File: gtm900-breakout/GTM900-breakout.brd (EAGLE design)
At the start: 70 x 70 mm, 97 parts, among them J1 AUDIO-JACK3, K1 PJ-002BH-SMT-TR, T1 BC847, T2 BC847, T3 BC847, T4 BC847, U1 FH12A-40S-0.5SH(55), U2 MCP1827T-ADJE/ET, U3 MIC5366, U4 CP2105-GM, U5 IP4234CZ6, X4 MINI-USB-SHIELD-UX60-MB-5ST

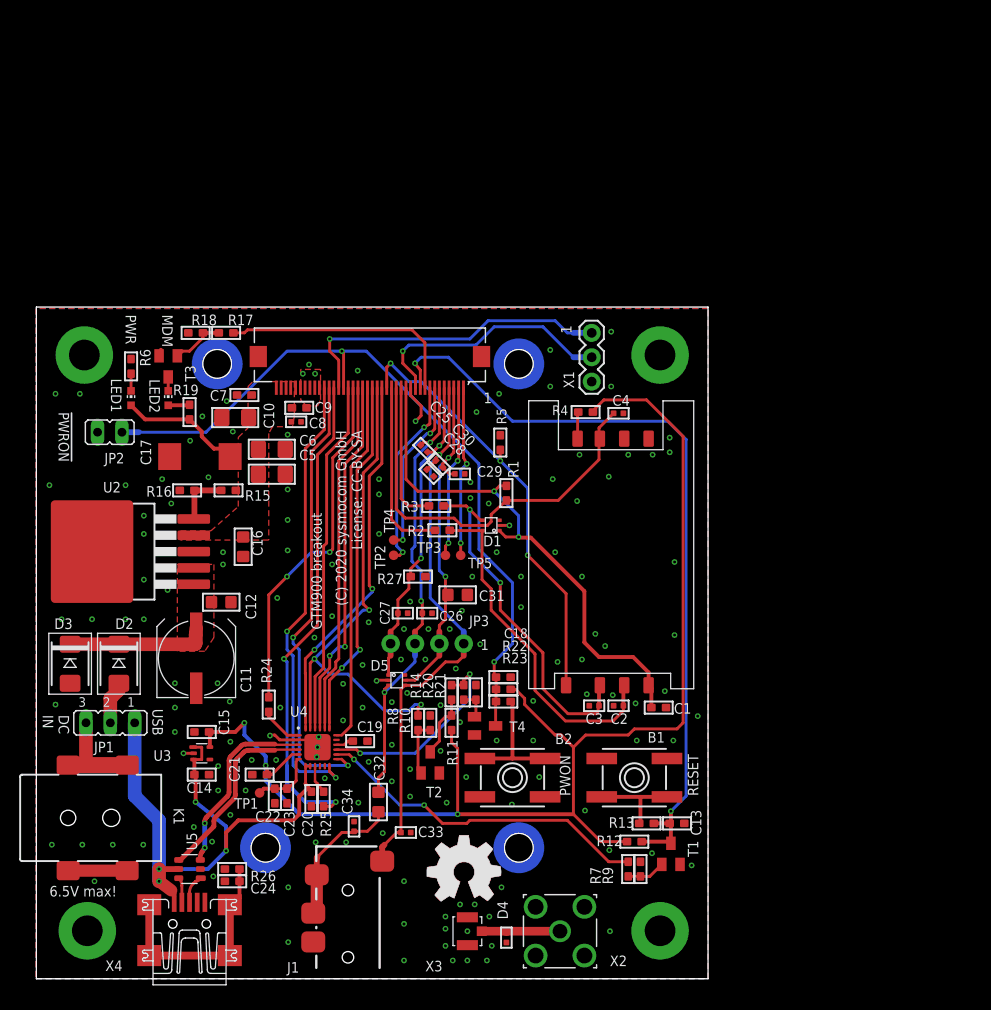
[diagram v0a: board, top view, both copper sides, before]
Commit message: GTM900-breakout: add next design v2
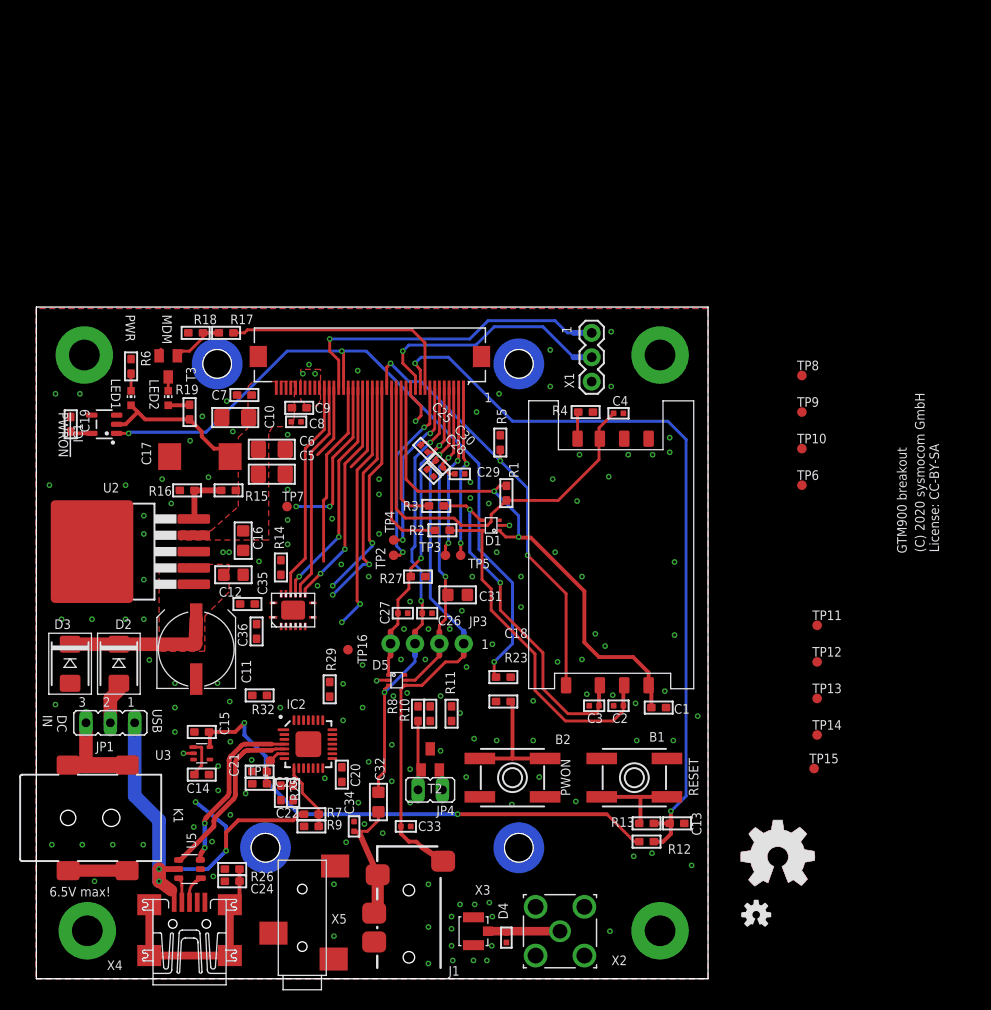
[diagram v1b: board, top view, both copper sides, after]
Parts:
- removed JP2: (no value), jumper:JP1
- removed R20, R21: 22k, rc-sysmocom:_0603
- removed R22: DNP, rc-sysmocom:_0603
- removed R24: 0, rc-sysmocom:_0603
- removed T1, T4: BC847, transistor:SOT23-BEC
- removed U4: CP2105-GM, usb-uart:QFN24_4X4
- added C35, C36: 100n, rc-sysmocom:_0603
- added IC1: NCP303, NCP303:SOT23-5
- added IC2: CP2102N_28, silabs_CP2102X:QFN28
- added JP4: (no value), jumper:JP1
- added R29: 4K7, rc-sysmocom:_0603
- added R32: 10k, rc-sysmocom:_0603
- added TP10, TP11, TP12, TP13, TP14, TP15, TP16, TP6, TP7, TP8, TP9: TPTP10R, testpad:TP10R
- added U$1: (no value), SparkFun-Aesthetics:OSHW-LOGO-S
- added U6: SN74AVC4T245-VQFN, laforge:VQFN-N16
- added X5: OsmoSer, laforge:JACK2.5_SJ-2523
- C19: value 4.7u -> 1u
- R25: value 4.7k -> 0
- R9: value 22k -> 47k
- moved C19 44.7 mm to (-22.5, 57.8), turned to 270 degrees
- moved R9 34.6 mm to (2.54, 15.9), turned to 0 degrees
- moved R7 33.5 mm to (2.54, 17.1), turned to 0 degrees
- moved U$3 32.7 mm to (51.1, 12.7)
- moved R14 22.0 mm to (-0.64, 42.9)
- moved J1 6.35 mm to (12.7, 0.64)
- moved R25 4.49 mm to (-0.64, 19.4)
- moved C20 4.07 mm to (5.71, 21.3)
- moved TP1 3.51 mm to (-1.75, 22.7)
- moved C23 3.13 mm to (-2.86, 20.3), turned to 0 degrees
- moved C12 3.13 mm to (-5.59, 42.1)
- moved C22 1.93 mm to (0.64, 19.4)
- moved R12 1.27 mm to (37.5, 14.3)
- moved R10 0.95 mm to (14.9, 27.6)
- moved R11 0.95 mm to (17.1, 27.6), turned to 90 degrees
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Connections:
- removed net GPIO.0_ECI/DTR_ECI: R14.2, R20.1, U4.15
- removed net GPIO.1_ECI/DSR_ECI: R7.1, U4.14
- removed net VCC: C10.2, C16.2, C17.+, C5.2, C6.2, C7.2, C8.1, C9.1, LED1.A, R15.2, R19.1, U1.36, U1.37, U1.38, U1.39, U1.40, U2.4
- removed net VDD_3V45: C22.1, C23.1, TP1.TP, U4.6
- new net CP_DTR: IC2.28, R8.1
- new net CP_VDD: C21.2, C23.2, C36.2, IC2.6, R29.1, R32.2, TP1.TP, U6.1, U6.2
- new net EN_VCC: R11.1, T2.C, U2.1, U3.3
- new net GPIO0/TXT: IC2.19
- new net GPIO1/RXT: IC2.18
- new net GPIO2/RS485: IC2.17
- new net GPIO3/WAKEUP: IC2.16
- new net GPIO4: IC2.22
- new net GPIO5: IC2.21
- new net GPIO6: IC2.20
- new net N$20: R32.1, U6.4, X5.2
- new net N$22: R14.1, U6.14, U6.15
- new net N$23: C19.2, IC1.5
- new net N$29: IC2.8, R7.2, R9.2
- new net N$30: IC2.27, TP15.TP
- new net N$32: IC2.1, TP14.TP
- new net VCC_4V1: C10.2, C16.2, C17.+, C5.2, C6.2, C7.2, C8.1, C9.1, IC1.2, LED1.A, R15.2, R19.1, U1.36, U1.37, U1.38, U1.39, U1.40, U2.4
- new net _UART_RXD: IC2.25, U6.5
- new net _UART_TXD: IC2.26, U6.7
- net !PWON: now also IC1.1; no longer JP2.1, R22.2, T4.C
- net !RST: no longer T1.C
- net GND: now also C20.1, C22.1, C23.1, C35.2, C36.1, IC1.3, IC2.3, IC2.EXP, JP4.2, R14.2, R9.1, U6.3, U6.8, U6.9, X5.1; no longer C20.2, C22.2, C23.2, JP2.2, R21.2, R9.2, T1.E, T4.E, U4.2, U4.25
- net LDO_IN: now also C14.2, C20.2, C22.2, R11.2, R25.2, U3.1; no longer U2.1
- net N$12: now also IC2.9, R29.2; no longer R25.1, U4.9
- net N$14: now also IC2.2, TP13.TP; no longer C19.2, U4.16
- net N$15: now also IC2.23, TP12.TP; no longer R24.2, U4.1
- net N$16: now also IC2.24, TP11.TP; no longer R20.2, R21.1, T4.B
- net N$17: now also IC2.7, R25.1; no longer R7.2, R9.1, T1.B
- net N$18: now also U6.6, X5.3; no longer R11.1, R14.1, T2.C
- net N$7: now also JP4.1
- net RXD2: now also U6.13; no longer U4.12
- net TXD2: now also U6.11; no longer U4.13
- net UART_CTS: now also TP10.TP; no longer U4.18
- net UART_DCD: now also TP6.TP; no longer U4.24
- net UART_DSR: now also TP9.TP; no longer U4.22
- net UART_DTR: now also TP16.TP; no longer R8.1, U4.23
- net UART_RI: now also TP7.TP; no longer R24.1
- net UART_RTS: now also TP8.TP; no longer U4.19
- net UART_RXD: now also U6.12; no longer U4.20
- net UART_TXD: now also U6.10; no longer U4.21
- net USB_D_N: now also IC2.5; no longer U4.4
- net USB_D_P: now also IC2.4; no longer U4.3
- net USB_VBUS: now also R7.1; no longer C14.2, C20.1, U3.1, U3.3, U4.7, U4.8
- net VDD: now also R4.2; no longer R25.2
- net VIO_2V8: now also C35.1, U6.16; no longer C21.2, R11.2, R22.1, R4.2, U4.5
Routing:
- net VIO_2V8: track 137.4 -> 54.2 mm, vias 3 -> 2
- net VDD: track 50.9 -> 7.69 mm, vias 2 -> 0
- net GPIO.1_ECI/DSR_ECI: track 35.3 -> 0.00 mm, vias 2 -> 0
- net UART_DTR: track 54.2 -> 24.4 mm, vias 3 -> 2
- net UART_CTS: track 37.9 -> 8.97 mm
- net RXD2: track 47.7 -> 22.9 mm, vias 2 -> 0
- net TXD2: track 47.4 -> 22.7 mm, vias 2 -> 0
- net GPIO.0_ECI/DTR_ECI: track 21.6 -> 0.00 mm, vias 2 -> 0
- net UART_RI: track 37.0 -> 16.9 mm
- net UART_DSR: track 36.9 -> 19.2 mm
- net UART_DCD: track 39.1 -> 23.0 mm
- net VCC_4V1: track 0.00 -> 16.0 mm
- net UART_TXD: track 37.7 -> 24.0 mm
- net USB_VBUS: track 62.6 -> 49.0 mm
- net VCC: track 13.3 -> 0.00 mm
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- added copper zone on layer 1, net VCC_4V1
- removed copper zone on layer 1, net VCC

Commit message: gtm900-bo: rename main files w/o explicit version
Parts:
- removed D5: PESD5V0UBV, laforge:SOT666
- removed JP4: (no value), jumper:JP1
- removed T3: BC847, transistor:SOT23-BEC
- removed TP11, TP12, TP13, TP14, TP15, TP16: TPTP10R, testpad:TP10R
- removed U$1: (no value), SparkFun-Aesthetics:OSHW-LOGO-S
- removed U5: IP4234CZ6, laforge:TSOP-6
- removed U6: SN74AVC4T245-VQFN, laforge:VQFN-N16
- removed X4: MINI-USB-SHIELD-UX60-MB-5ST, con-hirose:UX60-MB-5ST
- removed X5: OsmoSer, laforge:JACK2.5_SJ-2523
- added C37, C38, C39, C40, C41, C44, C45: 33p, rc-sysmocom:_0402
- added C42, C43: 10u, rc-sysmocom:_0805
- added IC3: TXB0102, TXB0102:VSSOP-8
- added JP2: (no value), jumper:JP2
- added L1, L2: 47nH, rc-sysmocom:_0603
- added R20: 22k, rc-sysmocom:_0603
- added R21, R22, R24: 220, rc-sysmocom:_0603
- added R28, R30: 1k, rc-sysmocom:_0603
- added R31: 0, rc-sysmocom:_0603
- added T1: BC847, transistor:SOT23-BEC
- added U4: RASPBERRY_PICOSMD, RpiPico:PICO-PKG-SMD
- C19: value 1u -> 33p; device rc-sysmocom:_0603 -> rc-sysmocom:_0402
- C20: value 1u -> 100n
- C21, C22, C36: value 100n -> 33p; device rc-sysmocom:_0603 -> rc-sysmocom:_0402
- C23: value 4.7u -> 100n
- C25, C30: value 33p -> 4.7u; device rc-sysmocom:_0402 -> rc-sysmocom:_0603
- C26, C28, C34: value 33p -> 100n; device rc-sysmocom:_0402 -> rc-sysmocom:_0603
- C31, C32: value 10u -> 100n; device rc-sysmocom:_0805 -> rc-sysmocom:_0603
- C35: value 100n -> 4.7u
- IC1: value NCP303 -> SN74AVC4T245-VQFN; device NCP303:SOT23-5 -> laforge:VQFN-N16
- IC2: value CP2102N_28 -> NAU88C10; device silabs_CP2102X:QFN28 -> NAU8810:QFN20
- JP1: device jumper:JP2 -> jumper:JP1
- R10, R16: value 22k -> 330
- R11: value 4.7k -> 200k
- R12: value DNP -> 22k
- R14: value 0 -> 22k
- R15: value 200k -> 22k
- R17: value 22k -> 0
- R18: value 22k -> 4,7k
- R19: value 330 -> 4,7k
- R23: value 1k -> 220
- R25: value 0 -> 220
- R26: value 1M -> 220
- R27: value 0 -> 1k
- R29: value 4K7 -> 22k
- R32: value 10k -> 0
- R6: value 330 -> 22k
- R8: value 22k -> 4.7k
- R9: value 47k -> 1k
- U2: value MCP1827T-ADJE/ET -> MIC5366; device ldo:TI_KTT_DPAK2 -> ldo:SC70-5
- U3: value MIC5366 -> MCP1827T-ADJE/ET; device ldo:SC70-5 -> ldo:TI_KTT_DPAK2
- moved J1 76.1 mm to (69.8, 51.0), turned to 180 degrees
- moved TP1 71.5 mm to (36.2, 83.3)
- moved T2 71.0 mm to (14.0, 93.8), turned to 180 degrees
- moved R12 70.0 mm to (15.9, 80.9), turned to 180 degrees
- moved R10 66.4 mm to (10.1, 93.8), turned to 270 degrees
- moved R9 66.2 mm to (63.7, 41.3), turned to 180 degrees
- moved C36 65.8 mm to (40.6, 85.2), turned to 135 degrees
- moved C24 64.7 mm to (42.2, 53.7)
- moved C19 62.1 mm to (37.1, 40.8)
- moved TP7 59.8 mm to (45.7, 87.8), turned to 180 degrees
- moved R14 58.2 mm to (20.0, 97.3), turned to 180 degrees
- moved R18 54.3 mm to (14.1, 18.4), turned to 90 degrees
- moved C32 54.2 mm to (47.9, 56.7), turned to 0 degrees
- moved R11 53.4 mm to (20.3, 80.9), turned to 0 degrees
- moved U3 53.2 mm to (6.03, 74.5), turned to 90 degrees
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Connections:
- net GPIO3/WAKEUP renamed SPKOUT-
- removed net CP_DTR: IC2.28, R8.1
- removed net CP_VDD: C21.2, C23.2, C36.2, IC2.6, R29.1, R32.2, TP1.TP, U6.1, U6.2
- removed net EN_VCC: R11.1, T2.C, U2.1, U3.3
- removed net GPIO0/TXT: IC2.19
- removed net GPIO1/RXT: IC2.18
- removed net GPIO2/RS485: IC2.17
- removed net GPIO4: IC2.22
- removed net GPIO5: IC2.21
- removed net GPIO6: IC2.20
- removed net N$23: C19.2, IC1.5
- removed net N$29: IC2.8, R7.2, R9.2
- removed net N$32: IC2.1, TP14.TP
- removed net USB_D_N: IC2.5, U5.4
- removed net USB_D_P: IC2.4, U5.3
- removed net _USB_DN: U5.6, X4.2
- removed net _USB_DP: U5.1, X4.3
- new net !MODEM_LDO_ON: R6.1, U4.P$19
- new net AGND: C25.1, C27.2, C28.2, C29.2, C30.2, C42.2, C44.1, C45.2, IC2.15, IC2.3, IC2.EXP, J1.4, R27.2, R28.2, R30.2, R31.1, R32.1
- new net MICBIAS: IC2.1
- new net MODEM_LDO_ON: R8.1, T1.C, U2.3, U3.1
- new net N$24: C27.1, C28.1, C30.1, IC2.2, L2.2
- new net N$25: C21.1, IC2.12, R18.1, R22.1
- new net N$26: C22.1, IC2.11, R19.1, R21.1
- new net N$28: C25.2, IC2.18
- new net N$31: C24.1, IC2.20
- new net PCM_CLK_RP2: R26.2, U4.P$14, U4.P$29
- new net PCM_FRAME_RP2: R25.2, U4.P$15
- new net PCM_MISO_RP2: R23.2, U4.P$17
- new net PCM_MOSI_RP2: R24.2, U4.P$16
- new net SCL: R21.2, U4.P$22
- new net SDA: R22.2, U4.P$21
- new net SPKOUT+: IC2.14
- new net SWGND: U4.P$42
- new net VCC: C23.2, C31.2, IC1.1, IC1.2, IC3.7, L1.1, L2.1, R18.2, R19.2, U4.P$36
- new net VSYS: U4.P$39
- new net _RXD2: IC1.4, U4.P$7
- new net _TXD2: IC1.6, U4.P$6
- new net _UART_CTS: IC3.1, U4.P$4
- new net _UART_RTS: IC3.8, U4.P$5
- net !PWON: now also R13.1, U4.P$9; no longer IC1.1, R23.1
- net !RST: now also R9.1; no longer R12.2, R13.1
- net AUXI+: now also TP5.TP; no longer TP3.TP
- net AUXI-: now also TP7.TP; no longer TP5.TP
- net AUXO+: now also TP4.TP; no longer TP2.TP
- net AUXO-: now also TP6.TP; no longer TP4.TP
- net EAR+: now also C36.2, C37.1, C43.2, R20.1; no longer C25.2, C26.1, C32.2, D5.3
- net EAR-: now also C36.1, C38.2, R32.2; no longer C25.1, C27.2, D5.1, R27.2
- net GND: now also C19.2, C20.2, C21.2, C22.2, C31.1, C34.2, C37.2, C38.1, C39.2, C40.2, IC1.8, IC1.9, IC2.5, IC3.2, JP1.2, R10.1, R12.2, R15.2, R17.2, R31.2, R7.2, T1.E, U2.2, U3.3, U3.PAD, U4.P$13, U4.P$18, U4.P$23, U4.P$28, U4.P$3, U4.P$33, U4.P$38, U4.P$8; no longer C19.1, C20.1, C21.1, C22.1, C24.1, C27.1, C28.2, C29.2, C31.2, C34.1, C36.1, D5.2, IC2.3, IC2.EXP, J1.4, JP4.2, R10.2, R14.2, R16.2, R18.2, R26.1, R27.1, R6.1, R9.1, T3.E, U2.3, U2.PAD, U3.2, U5.2, U6.3, U6.8, U6.9, X4.5, X5.1
- net LDO_IN: now also R8.2, U2.1, U3.2; no longer C20.2, C22.2, R11.2, R25.2, U2.2, U3.1
- net LPG: now also R14.1; no longer R17.1
- net MIC+: now also C32.1, C39.1, C41.1, C45.1; no longer C28.1, C30.1, C33.1, D5.4
- net MIC-: now also C40.1, C41.2, C42.1; no longer C29.1, C30.2, C31.1, D5.5
- net N$1: now also R10.2; no longer R6.2
- net N$11: now also C19.1, IC2.10, IC2.9, R26.1; no longer C24.2, R26.2, X4.M1, X4.M2, X4.M3, X4.M4
- net N$12: now also IC2.8, R25.1; no longer IC2.9, R29.2
- net N$14: now also IC2.7, R24.1; no longer IC2.2, TP13.TP
- net N$15: now also IC2.6, R23.1; no longer IC2.23, TP12.TP
- net N$16: now also C29.1, C32.2, R29.2, R30.1; no longer IC2.24, TP11.TP
- net N$17: now also JP1.1, R6.2, R7.1, T1.B; no longer IC2.7, R25.1
- net N$18: now also IC2.19, R28.1; no longer U6.6, X5.3
- net N$19: now also JP2.2; no longer JP1.2
- net N$2: now also R16.2; no longer R19.2
- net N$20: now also C33.1, C34.1, C35.1, IC2.17, IC2.4, L1.2; no longer R32.1, U6.4, X5.2
- net N$21: now also R9.2; no longer R13.2
- net N$22: now also IC1.14, IC1.15, R17.1; no longer R14.1, U6.14, U6.15
- net N$3: now also T2.C; no longer T3.C
- net N$30: now also IC2.13, R29.1; no longer IC2.27, TP15.TP
- net N$4: now also JP2.3; no longer JP1.3
- net N$5: now also R14.2, R15.1, T2.B; no longer R17.2, R18.1, T3.B
- net N$6: now also R11.1, R12.1, U3.5; no longer R15.1, R16.1, U2.5
- net N$7: now also C24.2, R20.2, R27.1; no longer JP4.1, R10.1, R8.2, T2.B
- net N$8: now also C43.1, C44.2; no longer C32.1, C34.2
- net N$9: now also R13.2; no longer R23.2
- net RXD2: now also IC1.13; no longer U6.13
- net TXD2: now also IC1.11; no longer U6.11
- net UART_CTS: now also IC3.4, TP8.TP; no longer TP10.TP
- net UART_DCD: now also TP1.TP; no longer TP6.TP
- net UART_DSR: now also TP10.TP; no longer TP9.TP
- net UART_DTR: now also TP9.TP; no longer TP16.TP
- net UART_RI: now also TP2.TP; no longer TP7.TP
- net UART_RTS: now also IC3.5, TP3.TP; no longer TP8.TP
- net UART_RXD: now also IC1.12; no longer U6.12
- net UART_TXD: now also IC1.10; no longer U6.10
- net USB_VBUS: now also JP2.1, U4.P$40; no longer JP1.1, R7.1, U5.5, X4.1
- net VCC_4V1: now also R11.2, R16.1, U3.4; no longer IC1.2, R15.2, R19.1, U2.4
- net VIO_2V8: now also C20.1, C26.1, IC1.16, IC3.3, IC3.6, U2.5; no longer C35.1, R12.1, U3.5, U6.16
- net _UART_RXD: now also IC1.5, U4.P$2; no longer IC2.25, U6.5
- net _UART_TXD: now also IC1.7, U4.P$1; no longer IC2.26, U6.7
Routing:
- net VCC: track 0.00 -> 131.9 mm, vias 0 -> 4
- net N$9: track 12.8 -> 86.8 mm, vias 0 -> 2
- net _UART_TXD: track 0.00 -> 63.9 mm, vias 0 -> 2
- net _UART_RXD: track 0.00 -> 61.2 mm, vias 0 -> 2
- net USB_VBUS: track 49.0 -> 107.2 mm, vias 4 -> 2
- net N$26: track 0.00 -> 54.4 mm, vias 0 -> 2
- net AGND: track 0.00 -> 54.3 mm, vias 0 -> 3
- net _TXD2: track 0.00 -> 54.0 mm, vias 0 -> 2
- net _RXD2: track 0.00 -> 53.5 mm, vias 0 -> 2
- net N$25: track 0.00 -> 52.1 mm, vias 0 -> 2
- net _UART_CTS: track 0.00 -> 47.5 mm, vias 0 -> 2
- net _UART_RTS: track 0.00 -> 46.5 mm, vias 0 -> 2
- net N$21: track 9.62 -> 50.1 mm, vias 0 -> 2
- net VDD: track 7.69 -> 43.3 mm, vias 0 -> 2
- net MODEM_LDO_ON: track 0.00 -> 31.3 mm, vias 0 -> 2
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- added copper zone on layer 1, net AGND
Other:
- board size 70 x 70 mm -> 70.2 x 100 mm
- board text added: "!PWON"
- board text added: "!RESET"
- board text added: "(C) 2023 sysmocom GmbH License: CC-BY-SA"
- board text removed: "!PWRON"
- board text removed: "(C) 2020 sysmocom GmbH License: CC-BY-SA"
- board text removed: "PWON"
- board text removed: "RESET"
